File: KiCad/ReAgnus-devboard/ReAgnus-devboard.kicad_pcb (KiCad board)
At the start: 4 copper layers, 63 x 100 mm, 7 parts, among them J3 Conn_01x01, J4 Conn_01x01, J5 Conn_01x01, J6 Conn_01x01, U1 PLCC-84-Plug, U2 ReAgnus_8375_socket, U3 Agnus_8375_socket

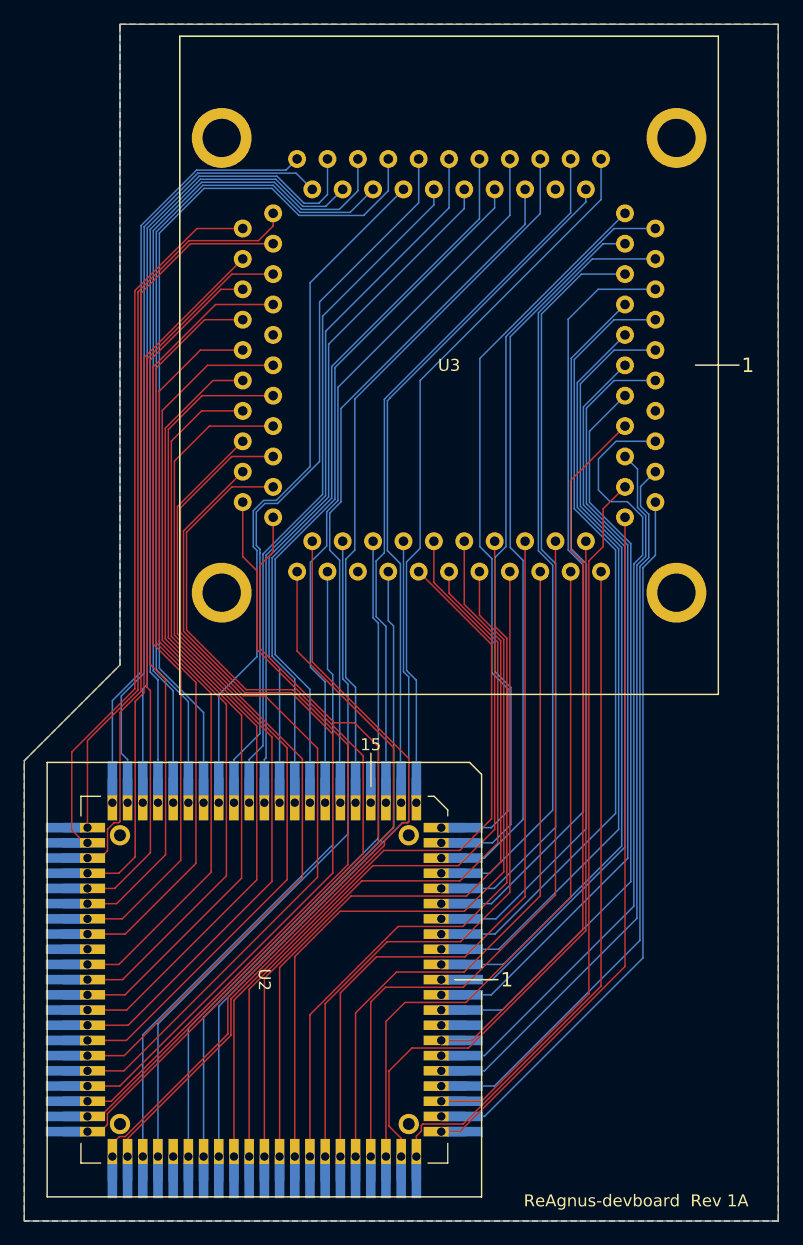
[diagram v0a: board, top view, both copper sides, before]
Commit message: added power jacks, rerouted with 6 mil tracks
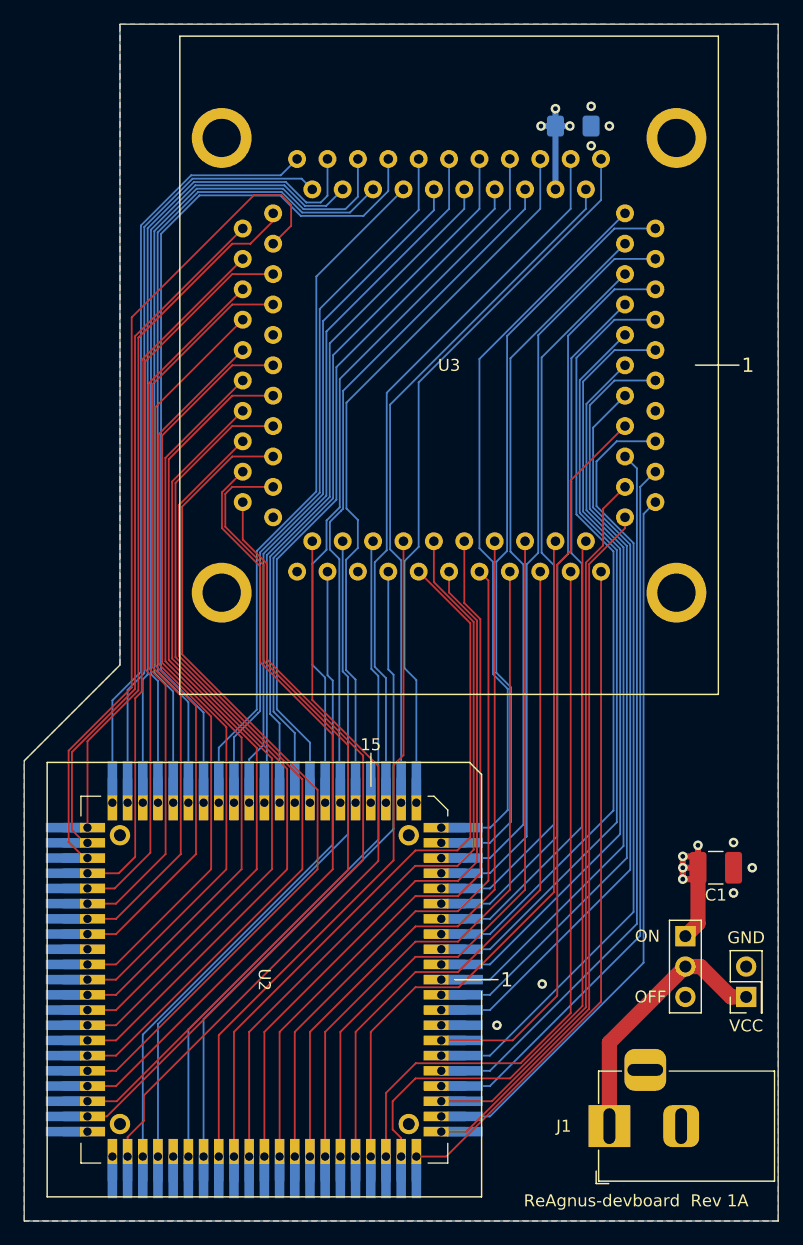
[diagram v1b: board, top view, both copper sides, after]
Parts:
- added C1: C, Capacitor_SMD:C_1210_3225Metric_Pad1.42x2.65mm_HandSolder, F.Cu at (175.1, 106.8)
- added C2: C_Small, Capacitor_SMD:C_1206_3216Metric_Pad1.42x1.75mm_HandSolder, B.Cu at (163.2, 44.8)
- added J1: Barrel_Jack_Switch, Connector_BarrelJack:BarrelJack_Horizontal, F.Cu at (166.2, 128.4)
- added J2: Conn_02x01, Connector_PinHeader_2.54mm:PinHeader_2x01_P2.54mm_Vertical, F.Cu at (177.6, 117.6)
- added SW1: SW_SPDT, Connector_PinHeader_2.54mm:PinHeader_1x03_P2.54mm_Vertical, F.Cu at (172.5, 112.5)
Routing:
- net VCC: track 1.98 -> 26.8 mm, vias 0 -> 7
- net /VIN: track 0.00 -> 22.1 mm
- net A20: track 64.6 -> 71.9 mm
- net DRA8: track 72.9 -> 67.8 mm
- net A7: track 65.0 -> 60.0 mm
- net A6: track 68.0 -> 63.0 mm
- net CASL: track 69.6 -> 64.6 mm
- net LDS: track 76.4 -> 71.7 mm
- net A5: track 65.4 -> 61.3 mm
- net A4: track 68.2 -> 64.6 mm
- net A3: track 66.0 -> 62.9 mm
- net DRA4: track 69.7 -> 67.0 mm
- net RGA1: track 63.1 -> 60.6 mm
- net DRD7: track 63.4 -> 60.9 mm
- net DRA9: track 66.7 -> 64.4 mm
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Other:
- board text added: "GND"
- board text added: "OFF"
- board text added: "ON"
- board text added: "VCC"
